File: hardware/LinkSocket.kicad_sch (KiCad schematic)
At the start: 4 parts, among them J1901 2x05_Horizontal, U1901 THVD24x2

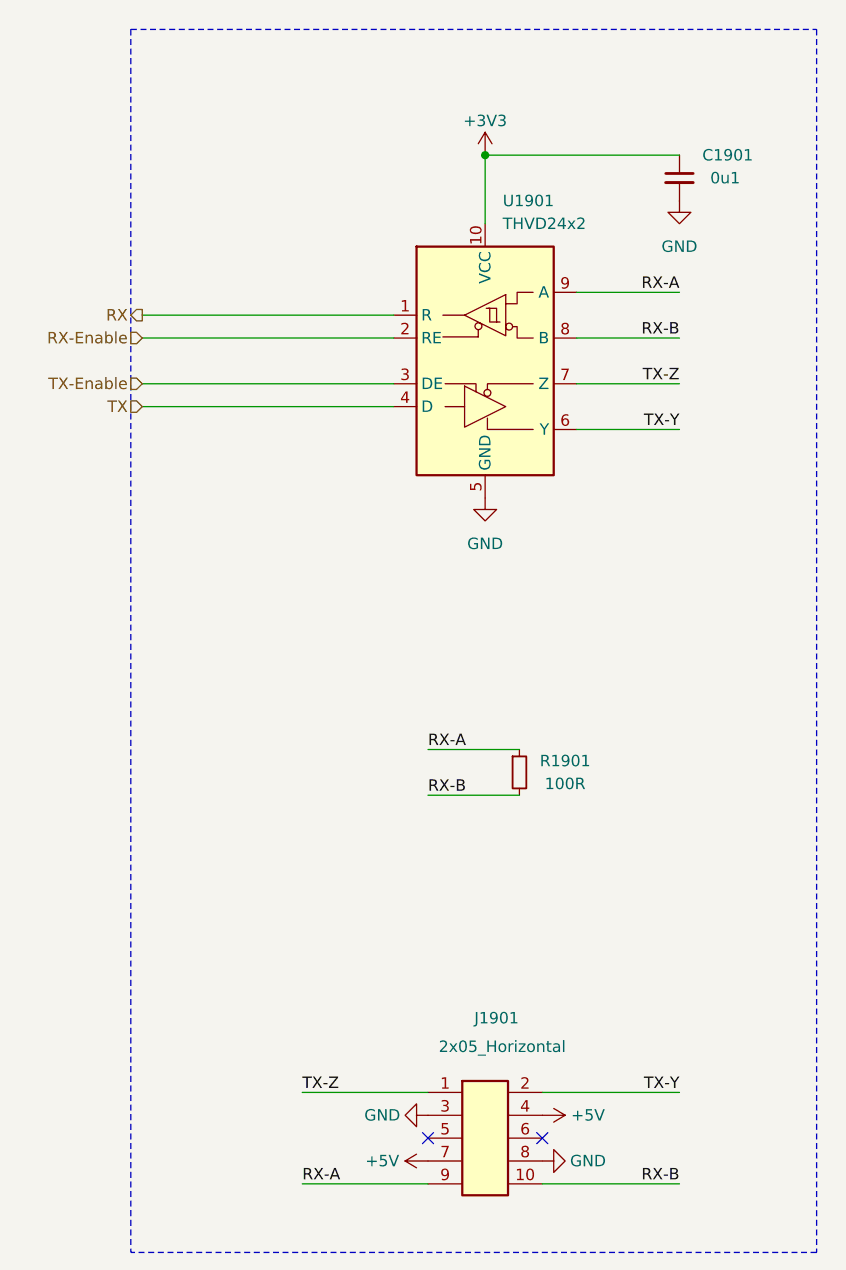
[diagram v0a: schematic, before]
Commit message: Replace Order_Number
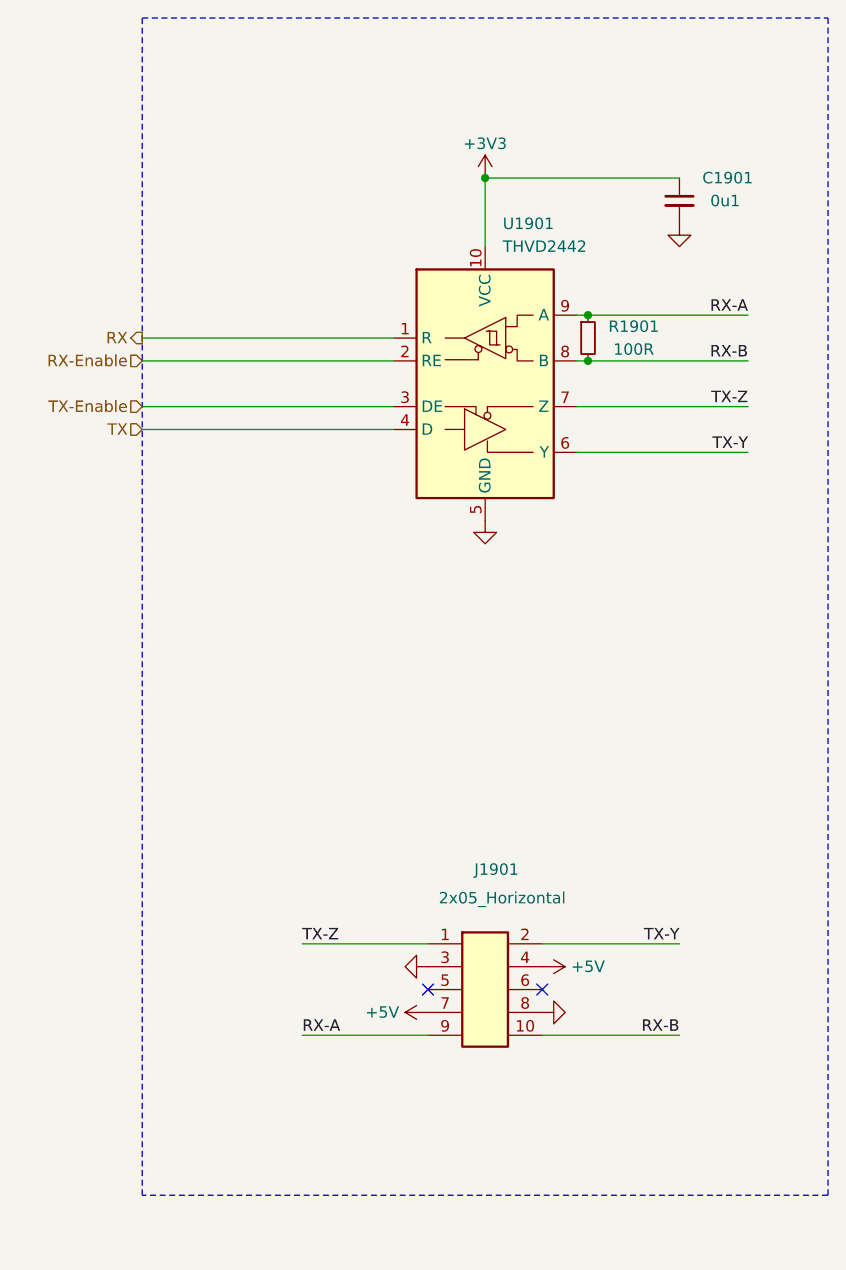
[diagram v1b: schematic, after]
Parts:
- C1901: footprint Capacitor_SMD:C_0603_1608Metric -> V2_Capacitor_SMD:C_0603; symbol Device:C_Small -> V2_Device:C_0603_0u1; Manufacturer (none) -> TDK; Mouser (none) -> 810-CGA3E2X7R1H104MA; Product (none) -> CGA3E2X7R1H104M080AA; Rating (none) -> 50V
- J1901: Manufacturer (none) -> Amphenol FCI; Mouser (none) -> 649-200211120001T4LF; Product (none) -> 20021112-00010T4LF
- R1901: footprint Resistor_SMD:R_0603_1608Metric -> V2_Resistor_SMD:R_0603; symbol Device:R_Small -> V2_Device:R_0603_100R; Manufacturer (none) -> Vishay; Mouser (none) -> 71-CRCW0603100RFKEAH; Product (none) -> CRCW0603100RFKEAHP; Rating (none) -> 330mW
- U1901: value THVD24x2 -> THVD2442; symbol V2_Interface_RS485:THVD24x2 -> V2_Interface_RS485:THVD2442; Manufacturer (none) -> Texas Instruments; Mouser (none) -> 595-THVD2442DRCR; Product (none) -> THVD2442DRCR
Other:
- moved on the sheet: C1901, J1901, R1901, U1901

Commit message: Update Library
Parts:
- C1901: symbol V2_Device:C_0603_0u1 -> V2_Capacitor:0603_0u1
- R1901: symbol V2_Device:R_0603_100R -> V2_Resistor:0603_100R
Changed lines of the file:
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@@
 		(on_board yes)
 		(dnp no)
-		(property "Reference" "#PWR01901"
+		(property "Reference" "#PWR1901"
 			(at 152.4 55.88 0)
 			(effects
@@
 			(project "express"
 				(path "/6c8448b4-b04d-47e1-934e-e40cbe27a7be/a5e4011d-0648-49f6-bc12-38b54bd48e3d"
-					(reference "#PWR01901")
+					(reference "#PWR1901")
 					(unit 1)
 				)
@@
 		(on_board yes)
 		(dnp no)
-		(property "Reference" "#PWR01904"
+		(property "Reference" "#PWR1904"
 			(at 139.7 139.7 0)
 			(effects
@@
 			(project "express"
 				(path "/6c8448b4-b04d-47e1-934e-e40cbe27a7be/a5e4011d-0648-49f6-bc12-38b54bd48e3d"
-					(reference "#PWR01904")
+					(reference "#PWR1904")
 					(unit 1)
 				)
@@
 		(on_board yes)
 		(dnp no)
-		(property "Reference" "#PWR01903"
+		(property "Reference" "#PWR1903"
 			(at 152.4 96.52 0)
 			(effects
@@
 			(project "express"
 				(path "/6c8448b4-b04d-47e1-934e-e40cbe27a7be/a5e4011d-0648-49f6-bc12-38b54bd48e3d"
-					(reference "#PWR01903")
+					(reference "#PWR1903")
 					(unit 1)
 				)
@@
 		(on_board yes)
 		(dnp no)
-		(property "Reference" "#PWR01902"
+		(property "Reference" "#PWR1902"
 			(at 173.99 63.5 0)
 			(effects
@@
 			(project "express"
 				(path "/6c8448b4-b04d-47e1-934e-e40cbe27a7be/a5e4011d-0648-49f6-bc12-38b54bd48e3d"
-					(reference "#PWR01902")
-					(unit 1)
-				)
-			)
-		)
-	)
-	(symbol
-		(lib_id "V2_Device:R_0603_100R")
+					(reference "#PWR1902")
+					(unit 1)
+				)
+			)
+		)
+	)
+	(symbol
+		(lib_id "V2_Resistor:0603_100R")
 		(at 163.83 69.85 0)
 		(unit 1)
@@
 		(on_board yes)
 		(dnp no)
-		(property "Reference" "#PWR01907"
+		(property "Reference" "#PWR1907"
 			(at 165.1 144.78 0)
 			(effects
@@
 			(project "express"
 				(path "/6c8448b4-b04d-47e1-934e-e40cbe27a7be/a5e4011d-0648-49f6-bc12-38b54bd48e3d"
-					(reference "#PWR01907")
+					(reference "#PWR1907")
 					(unit 1)
 				)
@@
 	)
 	(symbol
-		(lib_id "V2_Device:C_0603_0u1")
+		(lib_id "V2_Capacitor:0603_0u1")
 		(at 173.99 54.61 0)
 		(unit 1)
@@
 		(on_board yes)
 		(dnp no)
-		(property "Reference" "#PWR01906"
+		(property "Reference" "#PWR1906"
 			(at 149.86 144.78 0)
 			(effects
@@
 			(project "express"
 				(path "/6c8448b4-b04d-47e1-934e-e40cbe27a7be/a5e4011d-0648-49f6-bc12-38b54bd48e3d"
-					(reference "#PWR01906")
+					(reference "#PWR1906")
 					(unit 1)
 				)
@@
 		(on_board yes)
 		(dnp no)
-		(property "Reference" "#PWR01905"
+		(property "Reference" "#PWR1905"
 			(at 154.94 139.7 0)
 			(effects
@@
 			(project "express"
 				(path "/6c8448b4-b04d-47e1-934e-e40cbe27a7be/a5e4011d-0648-49f6-bc12-38b54bd48e3d"
-					(reference "#PWR01905")
-					(unit 1)
-				)
+					(reference "#PWR1905")
+					(unit 1)
+				)

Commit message: Replace diode
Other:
- title: V2 Link -> V2 express

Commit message: Update
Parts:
- C1901: Id (none) -> Capacitor:${SYMBOL_NAME}
- J1901: Id (none) -> Header:${SYMBOL_NAME}
- R1901: Id (none) -> Resistor:${SYMBOL_NAME}
- U1901: Id (none) -> RS485:${SYMBOL_NAME}
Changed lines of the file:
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@@
+			)
+		)
+		(property "Id" "RS485:${SYMBOL_NAME}"
+			(at 152.4 106.68 0)
+			(hide yes)
+			(show_name no)
+			(do_not_autoplace no)
+			(effects
+				(font
+					(size 1.27 1.27)
+				)
 			)
 		)
@@
 			)
 		)
+		(property "Id" "Resistor:${SYMBOL_NAME}"
+			(at 163.83 83.82 0)
+			(hide yes)
+			(show_name no)
+			(do_not_autoplace no)
+			(effects
+				(font
+					(size 1.27 1.27)
+				)
+			)
+		)
 		(pin "1"
 		)
@@
 			)
 		)
+		(property "Id" "Header:${SYMBOL_NAME}"
+			(at 152.4 157.48 0)
+			(hide yes)
+			(show_name no)
+			(do_not_autoplace no)
+			(effects
+				(font
+					(size 1.27 1.27)
+				)
+			)
+		)
 		(pin "1"
 		)
@@
 			(hide yes)
 			(show_name no)
+			(do_not_autoplace no)
+			(effects
+				(font
+					(size 1.27 1.27)
+				)
+			)
+		)
+		(property "Id" "Capacitor:${SYMBOL_NAME}"
+			(at 173.99 69.85 0)
+			(hide yes)
+			(show_name no)

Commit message: Update
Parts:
- J1901: Rating (none) -> 1A
- U1901: Rating (none) -> 20Mbps
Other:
- company: Socket -> Versio Duo
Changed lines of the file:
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@@
 	(title_block
 		(title "V2 express")
-		(date "2026-03-30")
-		(rev "2026-03-30")
-		(company "Socket")
+		(date "2026-04-14")
+		(rev "2026-04-14")
+		(company "Versio Duo")
+		(comment 1 "Expression Controller")
 	)
 	(rectangle
@@
 		(in_pos_files yes)
 		(dnp no)
-		(property "Reference" "#PWR1901"
+		(property "Reference" "#PWR01903"
 			(at 152.4 55.88 0)
 			(hide yes)
@@
 			(project "express"
 				(path "/6c8448b4-b04d-47e1-934e-e40cbe27a7be/a5e4011d-0648-49f6-bc12-38b54bd48e3d"
-					(reference "#PWR1901")
+					(reference "#PWR01903")
 					(unit 1)
 				)
@@
 			)
 		)
+		(property "Rating" "20Mbps"
+			(at 153.67 114.3 0)
+			(hide yes)
+			(show_name no)
+			(do_not_autoplace no)
+			(effects
+				(font
+					(size 1.27 1.27)
+				)
+			)
+		)
 		(pin "1"
 		)
@@
 		(in_pos_files yes)
 		(dnp no)
-		(property "Reference" "#PWR1904"
+		(property "Reference" "#PWR01901"
 			(at 139.7 139.7 0)
 			(hide yes)
@@
 			(project "express"
 				(path "/6c8448b4-b04d-47e1-934e-e40cbe27a7be/a5e4011d-0648-49f6-bc12-38b54bd48e3d"
-					(reference "#PWR1904")
+					(reference "#PWR01901")
 					(unit 1)
 				)
@@
 		(in_pos_files yes)
 		(dnp no)
-		(property "Reference" "#PWR1903"
+		(property "Reference" "#PWR01904"
 			(at 152.4 96.52 0)
 			(hide yes)
@@
 			(project "express"
 				(path "/6c8448b4-b04d-47e1-934e-e40cbe27a7be/a5e4011d-0648-49f6-bc12-38b54bd48e3d"
-					(reference "#PWR1903")
+					(reference "#PWR01904")
 					(unit 1)
 				)
@@
 		(in_pos_files yes)
 		(dnp no)
-		(property "Reference" "#PWR1902"
+		(property "Reference" "#PWR01907"
 			(at 173.99 63.5 0)
 			(hide yes)
@@
 			(project "express"
 				(path "/6c8448b4-b04d-47e1-934e-e40cbe27a7be/a5e4011d-0648-49f6-bc12-38b54bd48e3d"
-					(reference "#PWR1902")
+					(reference "#PWR01907")
 					(unit 1)
 				)
@@
 		(in_pos_files yes)
 		(dnp no)
-		(property "Reference" "#PWR1907"
+		(property "Reference" "#PWR01906"
 			(at 165.1 144.78 0)
 			(hide yes)
@@
 			(project "express"
 				(path "/6c8448b4-b04d-47e1-934e-e40cbe27a7be/a5e4011d-0648-49f6-bc12-38b54bd48e3d"
-					(reference "#PWR1907")
+					(reference "#PWR01906")
 					(unit 1)
 				)
@@
 			)
 		)
+		(property "Rating" "1A"
+			(at 152.4 172.72 0)
+			(hide yes)
+			(show_name no)
+			(do_not_autoplace no)
+			(effects
+				(font
+					(size 1.27 1.27)
+				)
+			)
+		)
 		(pin "1"
 		)
@@
 		(in_pos_files yes)
 		(dnp no)
-		(property "Reference" "#PWR1906"
+		(property "Reference" "#PWR01902"
 			(at 149.86 144.78 0)
 			(hide yes)
@@
 			(project "express"
 				(path "/6c8448b4-b04d-47e1-934e-e40cbe27a7be/a5e4011d-0648-49f6-bc12-38b54bd48e3d"
-					(reference "#PWR1906")
+					(reference "#PWR01902")
 					(unit 1)
 				)
@@
 		(in_pos_files yes)
 		(dnp no)
-		(property "Reference" "#PWR1905"
+		(property "Reference" "#PWR01905"
 			(at 154.94 139.7 0)
 			(hide yes)
@@
 			(project "express"
 				(path "/6c8448b4-b04d-47e1-934e-e40cbe27a7be/a5e4011d-0648-49f6-bc12-38b54bd48e3d"
-					(reference "#PWR1905")
+					(reference "#PWR01905")
 					(unit 1)
 				)

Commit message: Good Bye Imperial
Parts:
- C1901: footprint V2_Capacitor_SMD:C_0603 -> V2_Capacitor_SMD:C_1608; symbol V2_Capacitor:0603_0u1 -> V2_Capacitor:1608_0u1
- R1901: footprint V2_Resistor_SMD:R_0603 -> V2_Resistor_SMD:R_1608; symbol V2_Resistor:0603_100R -> V2_Resistor:1608_100R
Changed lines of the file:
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@@
 	)
 	(symbol
-		(lib_id "V2_Resistor:0603_100R")
+		(lib_id "V2_Resistor:1608_100R")
 		(at 163.83 69.85 0)
 		(unit 1)
@@
 			)
 		)
-		(property "Footprint" "V2_Resistor_SMD:R_0603"
+		(property "Footprint" "V2_Resistor_SMD:R_1608"
 			(at 163.83 85.598 0)
 			(hide yes)
@@
 	)
 	(symbol
-		(lib_id "V2_Capacitor:0603_0u1")
+		(lib_id "V2_Capacitor:1608_0u1")
 		(at 173.99 54.61 0)
 		(unit 1)
@@
 			)
 		)
-		(property "Footprint" "V2_Capacitor_SMD:C_0603"
+		(property "Footprint" "V2_Capacitor_SMD:C_1608"
 			(at 173.99 71.628 0)
 			(hide yes)
